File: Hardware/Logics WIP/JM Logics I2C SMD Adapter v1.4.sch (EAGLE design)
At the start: 30 parts, among them IC1 MEGA328P, J2 2.1MMJACK, X1 16.00MHz

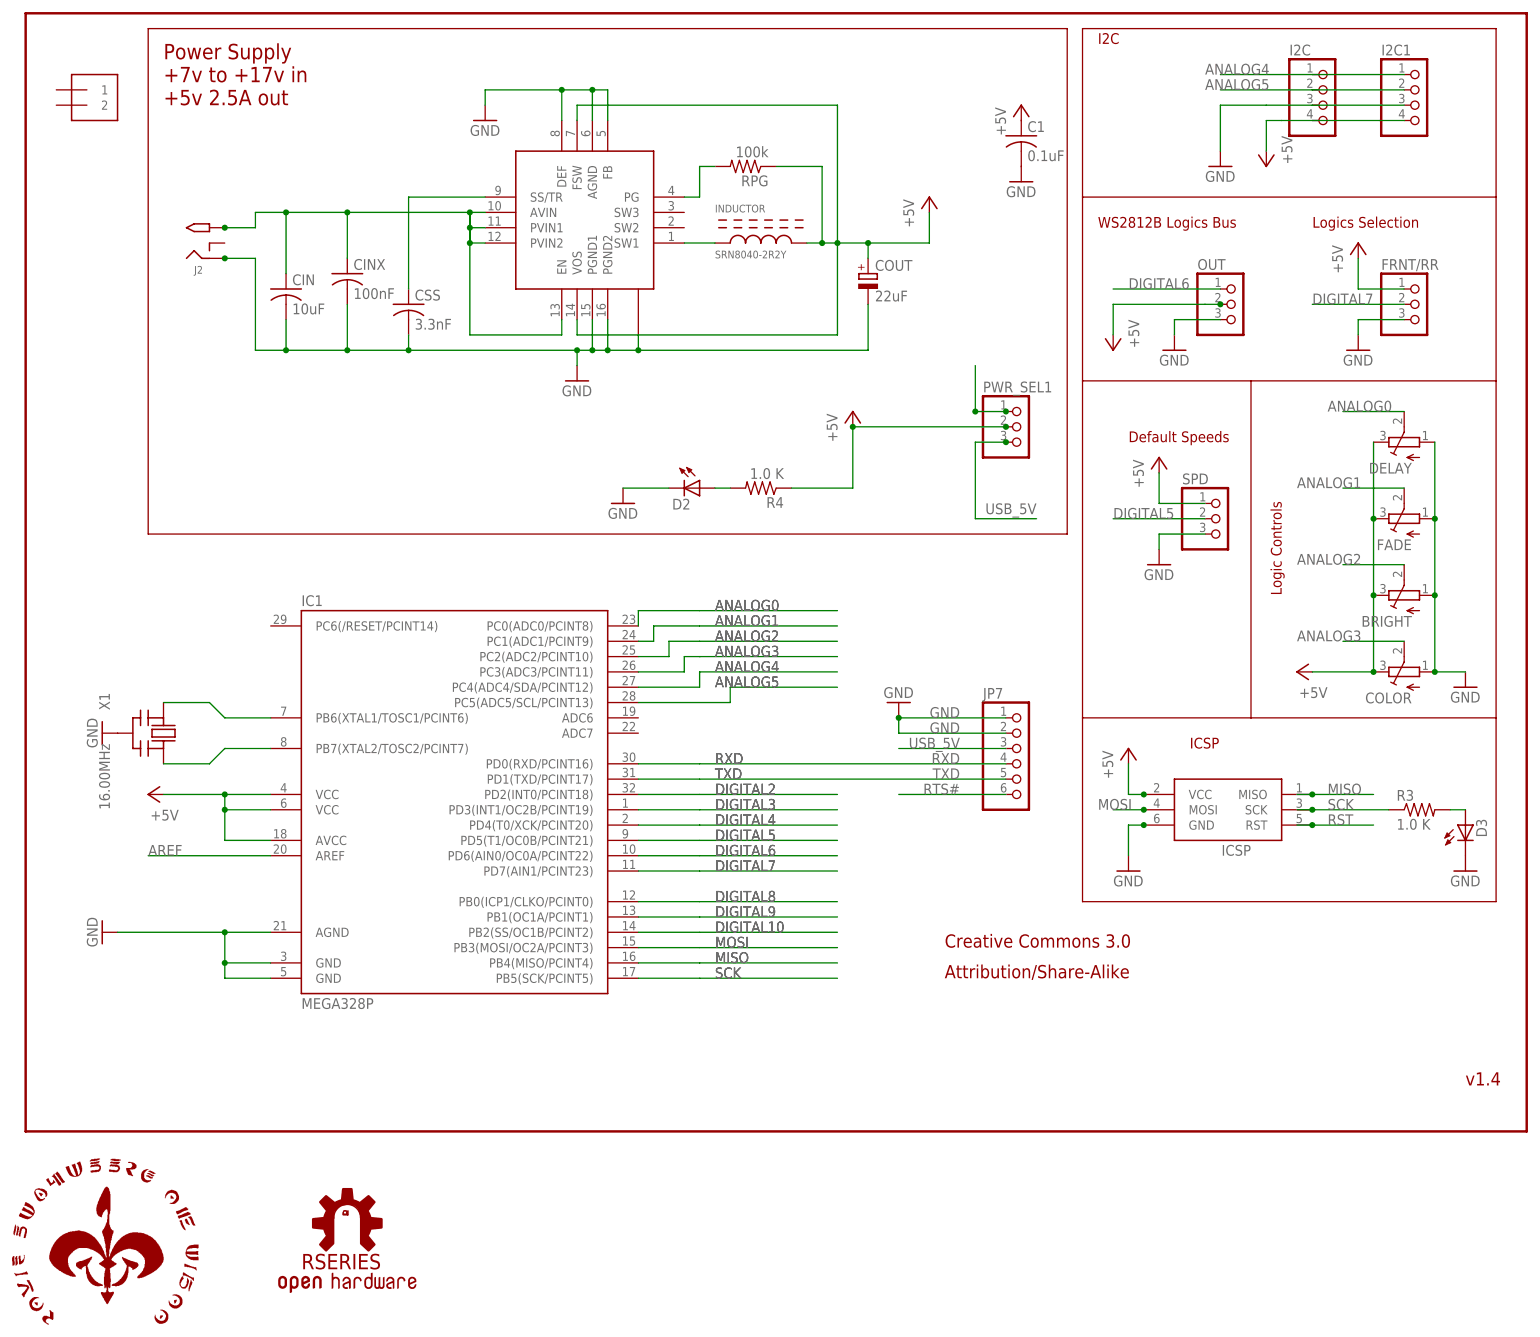
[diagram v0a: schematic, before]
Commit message: 
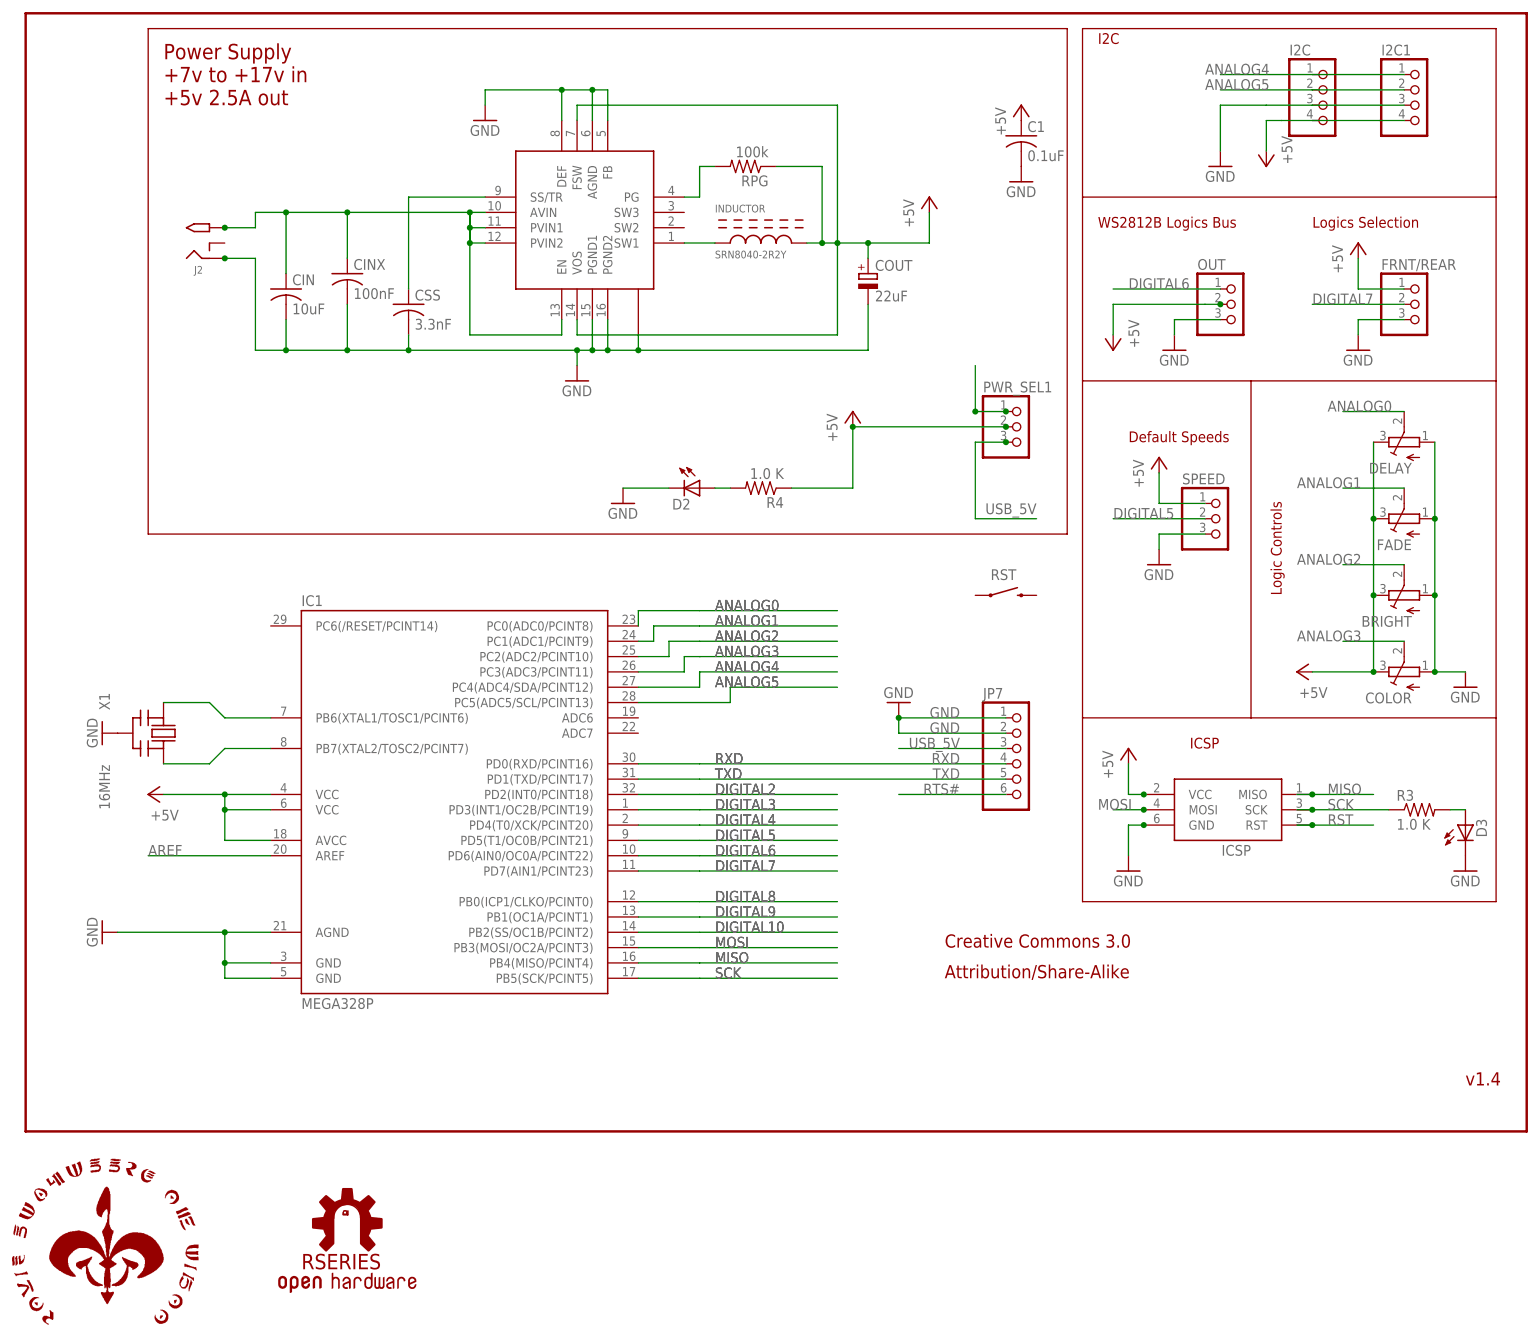
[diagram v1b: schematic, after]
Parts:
- removed 5VIN: 1X2-3.5MM, adafruit:1X2-3.5MM
- added RST: SWITCH-MOMENTARY-2SMD, SparkFun-Electromechanical:SWITCH-MOMENTARY-2SMD
- X1: value 16.00MHz -> 16MHz
- renumbered FRNT/RR to FRNT/REAR, SPD to SPEED
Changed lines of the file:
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@@
 <class number="0" name="default" width="0" drill="0">
 </class>
-<class number="1" name="supply" width="0.381" drill="0.1524">
-<clearance class="1" value="0.1524"/>
+<class number="1" name="supply" width="0.508" drill="0.1524">
+<clearance class="1" value="0.2032"/>
 </class>
 </classes>
 <parts>
 <part name="GND4" library="supply1" deviceset="GND" device=""/>
-<part name="X1" library="digg" deviceset="CERMOSCILL" device="" value="16.00MHz"/>
+<part name="X1" library="digg" deviceset="CERMOSCILL" device="" value="16MHz"/>
 <part name="GND10" library="supply1" deviceset="GND" device=""/>
 <part name="P+6" library="supply1" deviceset="+5V" device=""/>
@@
 <part name="U$1" library="rseries" deviceset="ROYAL-ENGINEERS-OF-NABOO" device="SMALL"/>
 <part name="OUT" library="pinhead" deviceset="PINHD-1X3" device=""/>
-<part name="FRNT/RR" library="pinhead" deviceset="PINHD-1X3" device=""/>
+<part name="FRNT/REAR" library="pinhead" deviceset="PINHD-1X3" device=""/>
 <part name="P+5" library="supply1" deviceset="+5V" device=""/>
 <part name="GND6" library="supply1" deviceset="GND" device=""/>
 <part name="DELAY" library="adafruit" deviceset="TRIMPOT" device="TC33X"/>
-<part name="SPD" library="pinhead" deviceset="PINHD-1X3" device=""/>
+<part name="SPEED" library="pinhead" deviceset="PINHD-1X3" device=""/>
 <part name="P+3" library="supply1" deviceset="+5V" device=""/>
 <part name="GND3" library="supply1" deviceset="GND" device=""/>
@@
 <part name="GND7" library="supply1" deviceset="GND" device=""/>
 <part name="P+7" library="supply1" deviceset="+5V" device=""/>
-<part name="5VIN" library="adafruit" deviceset="1X2" device="-3.5MM"/>
 <part name="REG" library="joymonkey" deviceset="TPS6213X" device="" value="TPS62133"/>
 <part name="CIN" library="adafruit" deviceset="C-US" device="C0805K" value="10uF"/>
@@
 <part name="P+4" library="supply1" deviceset="+5V" device=""/>
 <part name="GND9" library="supply1" deviceset="GND" device=""/>
+<part name="RST" library="SparkFun-Electromechanical" deviceset="SWITCH-MOMENTARY-2" device="SMD" value=""/>
 </parts>
 <sheets>
@@
 <instance part="U$1" gate="G$1" x="-2.54" y="-33.02"/>
 <instance part="OUT" gate="A" x="200.66" y="137.16"/>
-<instance part="FRNT/RR" gate="A" x="231.14" y="137.16"/>
+<instance part="FRNT/REAR" gate="A" x="231.14" y="137.16"/>
 <instance part="P+5" gate="1" x="220.98" y="147.32"/>
 <instance part="GND6" gate="1" x="220.98" y="129.54"/>
@@
 <attribute name="VALUE" x="232.41" y="110.49" size="1.778" layer="96" rot="R180"/>
 </instance>
-<instance part="SPD" gate="A" x="198.12" y="101.6"/>
+<instance part="SPEED" gate="A" x="198.12" y="101.6"/>
 <instance part="P+3" gate="1" x="187.96" y="111.76"/>
 <instance part="GND3" gate="1" x="187.96" y="93.98"/>
@@
 <instance part="GND7" gate="1" x="238.76" y="73.66"/>
 <instance part="P+7" gate="1" x="210.82" y="76.2" rot="R90"/>
-<instance part="5VIN" gate="G$1" x="10.16" y="170.18"/>
 <instance part="REG" gate="G$1" x="83.82" y="149.86" rot="R180"/>
 <instance part="CIN" gate="G$1" x="43.18" y="139.7"/>
@@
 <attribute name="VALUE" x="73.66" y="165.1" size="1.778" layer="96"/>
 </instance>
+<instance part="RST" gate="G$1" x="162.56" y="88.9"/>
 </instances>
 <busses>
@@
 </segment>
 <segment>
-<pinref part="FRNT/RR" gate="A" pin="3"/>
+<pinref part="FRNT/REAR" gate="A" pin="3"/>
 <pinref part="GND6" gate="1" pin="GND"/>
 <wire x1="228.6" y1="134.62" x2="220.98" y2="134.62" width="0.1524" layer="91"/>
@@
 </segment>
 <segment>
-<pinref part="SPD" gate="A" pin="3"/>
+<pinref part="SPEED" gate="A" pin="3"/>
 <pinref part="GND3" gate="1" pin="GND"/>
 <wire x1="195.58" y1="99.06" x2="187.96" y2="99.06" width="0.1524" layer="91"/>
@@
 </segment>
 <segment>
-<pinref part="FRNT/RR" gate="A" pin="1"/>
+<pinref part="FRNT/REAR" gate="A" pin="1"/>
 <pinref part="P+5" gate="1" pin="+5V"/>
 <wire x1="228.6" y1="139.7" x2="220.98" y2="139.7" width="0.1524" layer="91"/>
@@
 </segment>
 <segment>
-<pinref part="SPD" gate="A" pin="1"/>
+<pinref part="SPEED" gate="A" pin="1"/>
 <pinref part="P+3" gate="1" pin="+5V"/>
 <wire x1="195.58" y1="104.14" x2="187.96" y2="104.14" width="0.1524" layer="91"/>
@@
 </segment>
 <segment>
-<pinref part="FRNT/RR" gate="A" pin="2"/>
+<pinref part="FRNT/REAR" gate="A" pin="2"/>
 <wire x1="228.6" y1="137.16" x2="213.36" y2="137.16" width="0.1524" layer="91"/>
 <label x="213.36" y="137.16" size="1.778" layer="95"/>
@@
 </segment>
 <segment>
-<pinref part="SPD" gate="A" pin="2"/>
+<pinref part="SPEED" gate="A" pin="2"/>
 <wire x1="195.58" y1="101.6" x2="180.34" y2="101.6" width="0.1524" layer="91"/>
 <label x="180.34" y="101.6" size="1.778" layer="95"/>

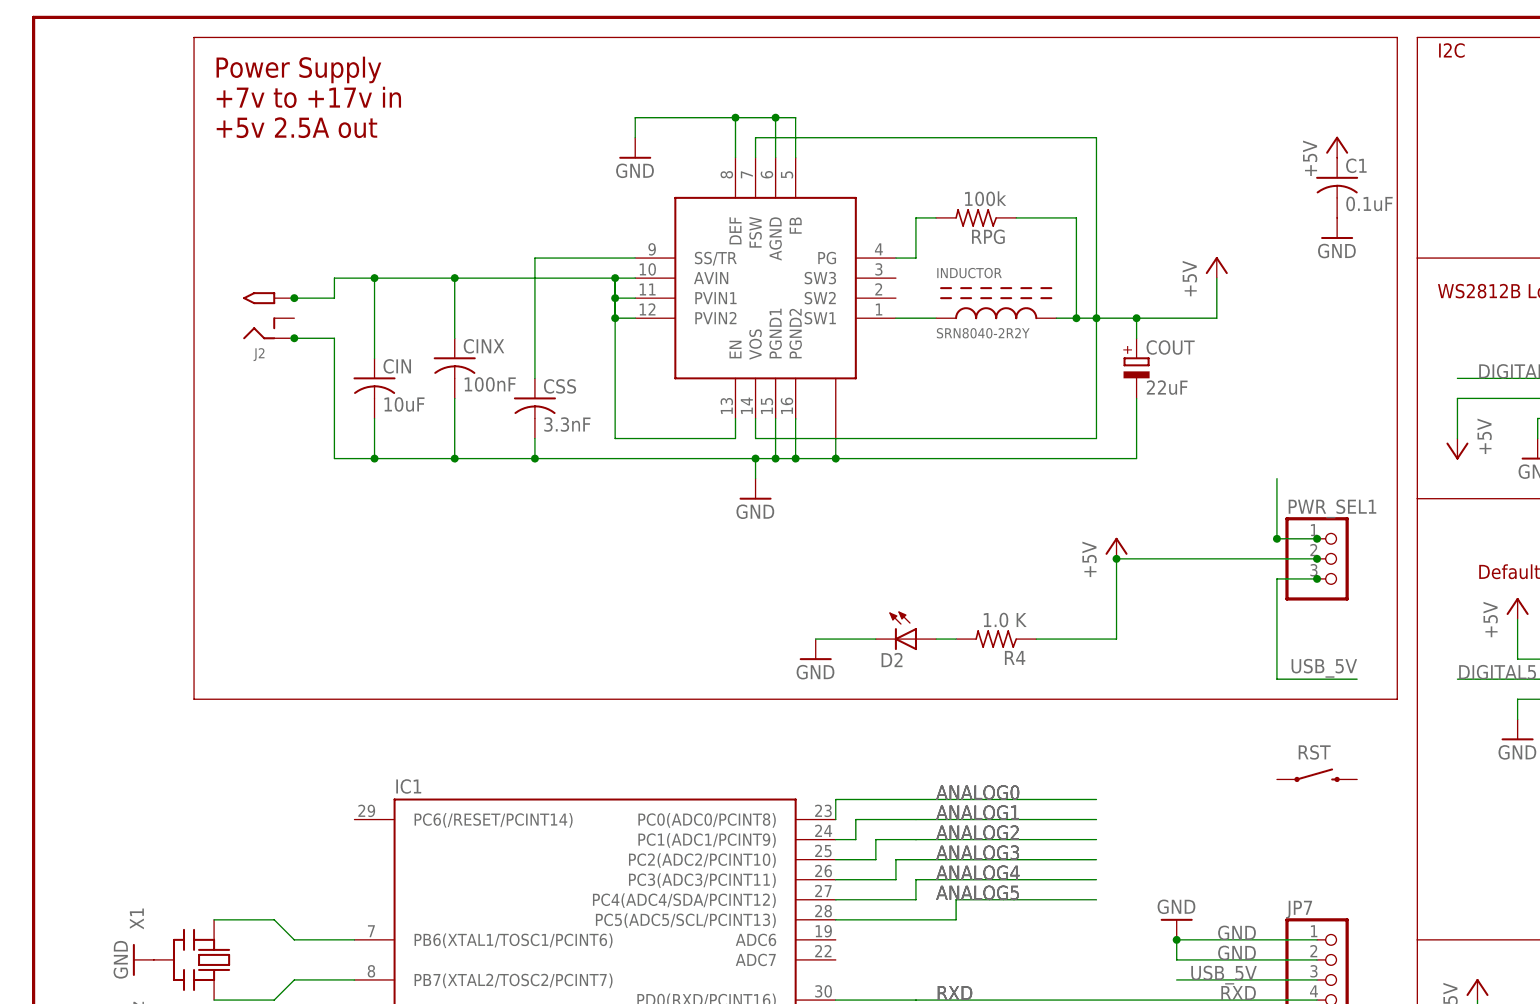
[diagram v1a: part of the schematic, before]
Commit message: Need to repackage inductor on Logic Engine to include GND (duh!)
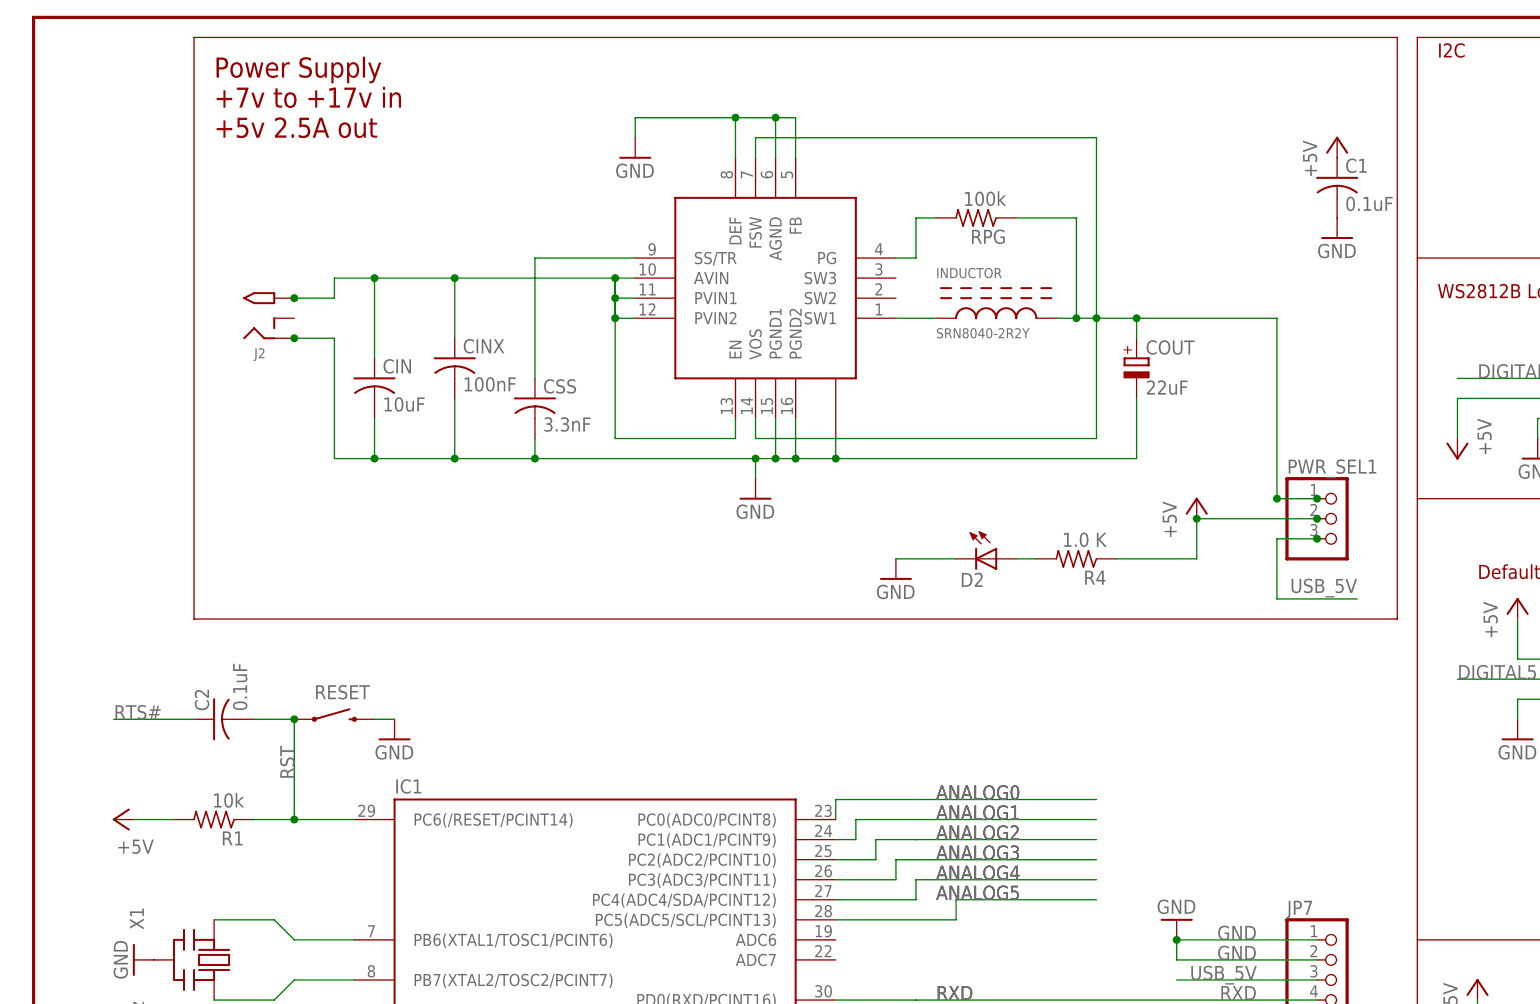
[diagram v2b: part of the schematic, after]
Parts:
- removed RST: SWITCH-MOMENTARY-2SMD, SparkFun-Electromechanical:SWITCH-MOMENTARY-2SMD
- added C2: 0.1uF, adafruit:C-USC0805K
- added R1: 10k, adafruit:R-US_R0805
- added RESET: SWITCH-MOMENTARY-2SMD, SparkFun-Electromechanical:SWITCH-MOMENTARY-2SMD
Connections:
- net +5V: now also R1.2; no longer COUT.+, INDUCTOR.P2, REG.FSW, REG.VOS, RPG.1
- net GND: now also RESET.2
- net N$9: now also COUT.+, INDUCTOR.P2, REG.FSW, REG.VOS, RPG.1
- net RST: now also C2.2, IC1.PC6(/RESET/PCINT14), R1.1, RESET.1
- net RTS#: now also C2.1
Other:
- moved on the sheet: D2, PWR_SEL1, R4
